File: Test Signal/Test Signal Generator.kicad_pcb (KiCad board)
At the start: 2 copper layers, 41.9 x 33 mm, 11 parts, among them U1 TL072

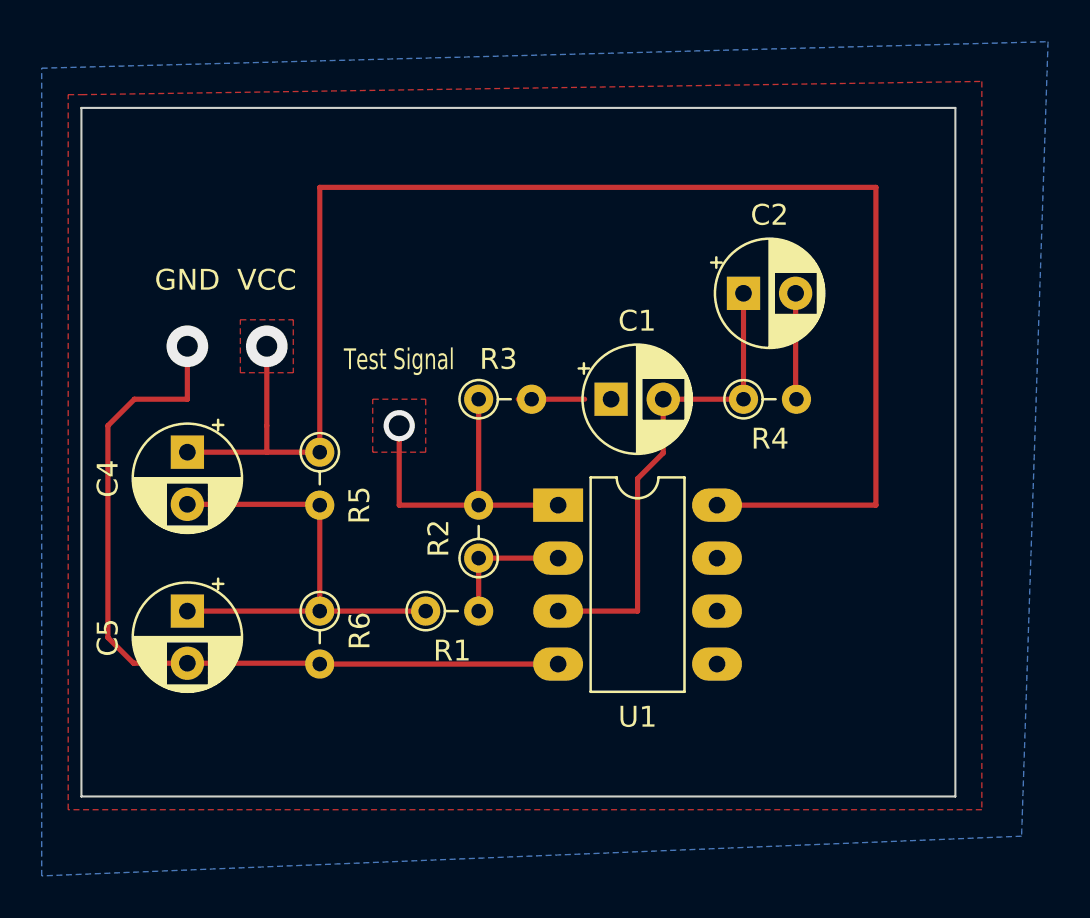
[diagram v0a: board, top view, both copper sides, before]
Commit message: schematics updated, pcb updated
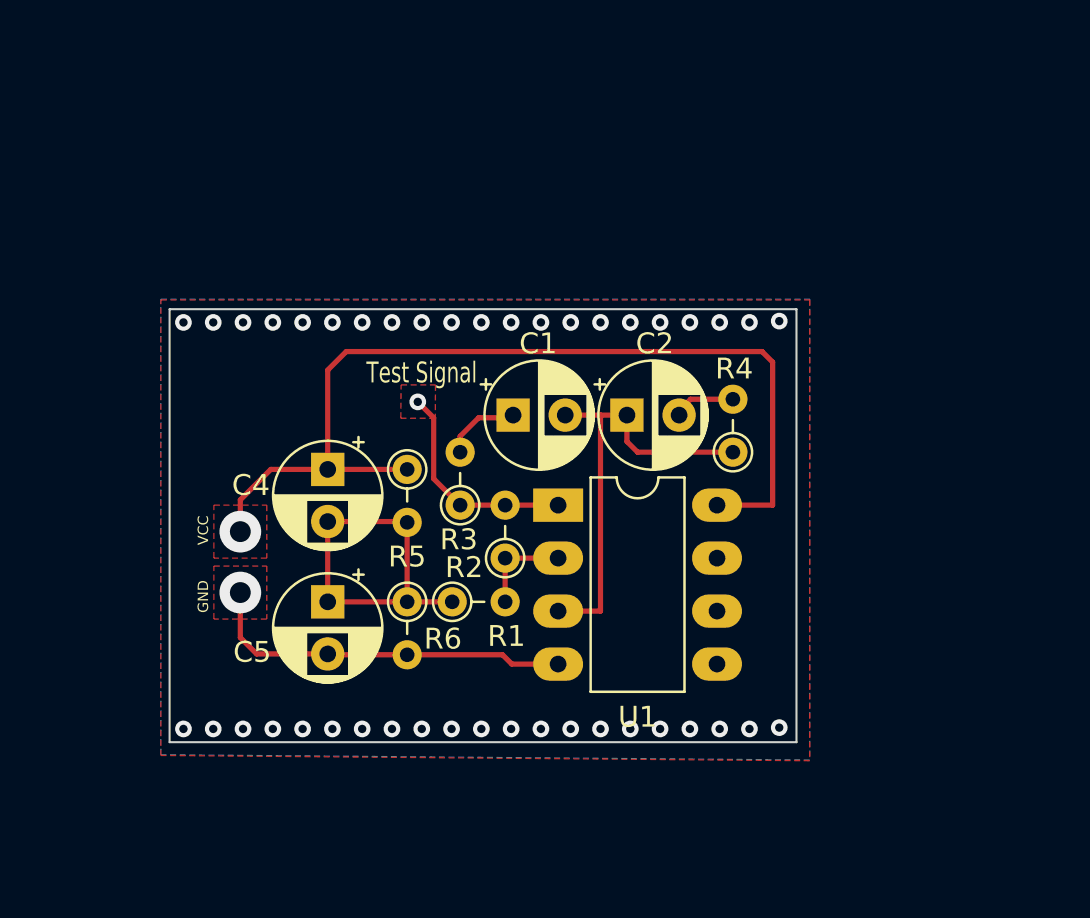
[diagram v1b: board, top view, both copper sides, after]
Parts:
- R2: value 3.9k -> 2k
- moved C2 8.08 mm to (120.1, 70.6)
- moved C4 6.78 mm to (105.8, 73.2)
- moved C5 6.75 mm to (105.8, 79.6)
- moved R3 5.16 mm to (112.1, 74.9), turned to 90 degrees
- moved C1 4.76 mm to (114.7, 70.6)
- moved R5 4.27 mm to (109.6, 73.2)
- moved R6 4.21 mm to (109.6, 79.6)
- moved R4 2.59 mm to (125.2, 72.4), turned to 90 degrees
- moved R1 1.35 mm to (111.8, 79.6)
- moved R2 1.27 mm to (114.3, 77.5)
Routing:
- net +5V: track 73.7 -> 46.3 mm
- net -VDC: track 39.2 -> 17.9 mm, vias 1 -> 43
- net Test_Signal: track 16.5 -> 10.5 mm
- net GNDREF: track 22.9 -> 17.5 mm
- net Net-(C1-Pad2): track 23.4 -> 21.0 mm
- net Net-(C2-Pad2): track 5.10 -> 3.02 mm
- net Net-(R1-Pad2): track 6.35 -> 4.64 mm
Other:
- board size 41.9 x 33 mm -> 30.1 x 20.8 mm
